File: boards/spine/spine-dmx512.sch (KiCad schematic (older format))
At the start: 27 parts, among them P2 XLR-3 Female, Q1 IRFML8244, Q2 IRFML8244, T1 10/100baseT transformer, U3 NC7WZ14, U4 NC7WZ14, U5 NC7WZ14, U6 SN75176B

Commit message: Power management and such
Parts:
- D4: value TVS 20V -> 8.5VWM; MfgId MMBZ20VALT1G -> MMBZ12VALT1G; RefPrice1k .04208 -> .04471; Vend1Id MMBZ20VALT1GOSCT-ND -> MMBZ12VALT1GOSCT-ND
- gave numbers to parts that had none: 1
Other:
- moved on the sheet: C18, C19, C20, C21, C22, C23, C24, C25, C26, C27, C28, C29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

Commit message: Clock generator, sync connectors, title blocks
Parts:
- C18, C19, C21, C22, C23, C24, C25, C26, C28: footprint 0805 -> Capacitors_SMD:C_0805
- C20, C27: footprint 1206 -> Capacitors_SMD:C_1206
- R11, R12, R13, R14: footprint (none) -> Resistors_SMD:R_0805
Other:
- note added: "A"
- note added: "Wiggle Spine board"

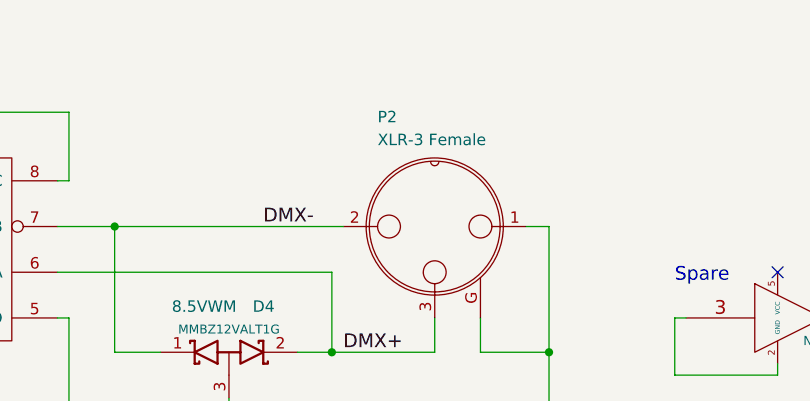
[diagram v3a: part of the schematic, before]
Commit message: Schematic footprint and refdes work
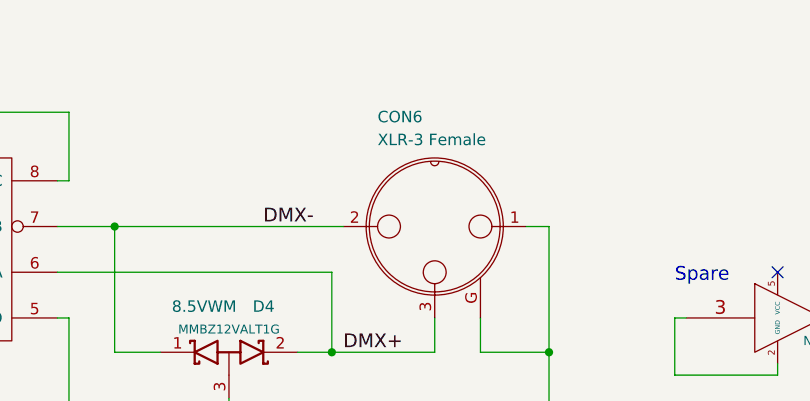
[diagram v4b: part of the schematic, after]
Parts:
- C29: footprint (none) -> Capacitors_ThroughHole:C_Rect_L13_W4_P10
- CON6: renamed from P2; footprint (none) -> Connect:XLR3MC
- D2, D3, D4, Q1, Q2: footprint (none) -> TO_SOT_Packages_SMD:SOT-23
- T1: footprint (none) -> Housings_SOIC:SOIC-16_7.5x10.3mm_Pitch1.27mm
- U3, U4, U5: footprint (none) -> TO_SOT_Packages_SMD:SC-70-6
- U6: footprint (none) -> Housings_SOIC:SOIC-8_3.9x4.9mm_Pitch1.27mm
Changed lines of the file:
@@
 F 0 "U6" H 5700 1350 60  0000 L BNN
 F 1 "SN75176B" H 5700 450 60  0000 L TNN
-F 2 "" H 6000 1300 60  0001 C CNN
+F 2 "Housings_SOIC:SOIC-8_3.9x4.9mm_Pitch1.27mm" H 6000 1300 60  0001 C CNN
 F 3 "http://www.ti.com/lit/ds/symlink/sn65176b.pdf" H 6000 1300 60  0001 C CNN
 F 4 "296-1275-1-ND" H 6000 1300 60  0001 C CNN "Vend1Id"
@@
 F 0 "T1" H 7650 4500 50  0000 L BNN
 F 1 "10/100baseT transformer" H 7650 4500 50  0001 L BNN
-F 2 "" H 8000 4450 50  0001 C CNN
+F 2 "Housings_SOIC:SOIC-16_7.5x10.3mm_Pitch1.27mm" H 8000 4450 50  0001 C CNN
 F 3 "http://www.mouser.com/ds/2/54/PT61018PEL-336005.pdf" H 8000 4300 60  0001 C CNN
 F 4 "Bourns" H 8050 4250 60  0001 C CNN "MfrId"
@@
 F 0 "U4" H 4750 2100 40  0000 C CNN
 F 1 "NC7WZ14" H 4800 1900 40  0000 C CNN
-F 2 "" H 4600 2000 60  0001 C CNN
+F 2 "TO_SOT_Packages_SMD:SC-70-6" H 4600 2000 60  0001 C CNN
 F 3 "http://www.fairchildsemi.com/datasheets/NC/NC7WZ14.pdf" H 4600 2000 60  0001 C CNN
 F 4 "0.07631" H 4600 2000 60  0001 C CNN "RefPrice1k"
@@
 F 0 "D3" V 2400 1850 50  0000 C CNN
 F 1 "BAT54 2x common cathode" H 2500 2100 50  0001 C CNN
-F 2 "" H 2500 2000 60  0001 C CNN
+F 2 "TO_SOT_Packages_SMD:SOT-23" H 2500 2000 60  0001 C CNN
 F 3 "http://www.diodes.com/_files/datasheets/ds11005.pdf" H 2500 2000 60  0001 C CNN
 F 4 "Diodes Inc" H 2500 2150 39  0001 C CNN "MfrId"
@@
 F 0 "Q1" H 5850 4500 50  0000 R CNN
 F 1 "IRFML8244" H 6150 4400 50  0001 R CNN
-F 2 "" H 5750 4550 29  0001 C CNN
+F 2 "TO_SOT_Packages_SMD:SOT-23" H 5750 4550 29  0001 C CNN
 F 3 "http://www.irf.com/product-info/datasheets/data/irfml8244pbf.pdf" H 5550 4450 60  0001 C CNN
 F 4 "Infineon" H 5550 4450 60  0001 C CNN "MfrId"
@@
 $EndComp
 $Comp
-L GND #PWR018
+L GND #PWR19
 U 1 1 563F2AEF
 P 2650 6250
-F 0 "#PWR018" H 2650 6000 50  0001 C CNN
+F 0 "#PWR19" H 2650 6000 50  0001 C CNN
 F 1 "GND" H 2650 6100 50  0000 C CNN
 F 2 "" H 2650 6250 60  0000 C CNN
@@
 $EndComp
 $Comp
-L +5V #PWR019
+L +5V #PWR18
 U 1 1 563F515D
 P 2650 3550
-F 0 "#PWR019" H 2650 3400 50  0001 C CNN
+F 0 "#PWR18" H 2650 3400 50  0001 C CNN
 F 1 "+5V" H 2650 3690 50  0000 C CNN
 F 2 "" H 2650 3550 60  0000 C CNN
@@
 F 0 "Q2" H 6250 4950 50  0000 R CNN
 F 1 "IRFML8244" H 6550 4850 50  0001 R CNN
-F 2 "" H 6150 5000 29  0001 C CNN
+F 2 "TO_SOT_Packages_SMD:SOT-23" H 6150 5000 29  0001 C CNN
 F 3 "http://www.irf.com/product-info/datasheets/data/irfml8244pbf.pdf" H 5950 4900 60  0001 C CNN
 F 4 "Infineon" H 5950 4900 60  0001 C CNN "MfrId"
@@
 $EndComp
 $Comp
-L XLR_3 P2
+L XLR_3 CON6
 U 1 1 563E82C1
 P 8050 1600
-F 0 "P2" H 7800 2050 50  0000 L BNN
+F 0 "CON6" H 7800 2050 50  0000 L BNN
 F 1 "XLR-3 Female" H 7800 1950 50  0000 L BNN
-F 2 "" H 8050 1600 60  0001 C CNN
+F 2 "Connect:XLR3MC" H 8050 1600 60  0001 C CNN
 F 3 "http://www.neutrik.us/en-us/xlr/aa-series/nc3faah2-0" H 8050 1600 60  0001 C CNN
 F 4 "568-NC3FAAH-2-O" H 8050 1600 60  0001 C CNN "Vend1Id"
@@
 F 0 "U4" H 9750 2100 40  0000 C CNN
 F 1 "NC7WZ14" H 9800 1900 40  0000 C CNN
-F 2 "" H 9600 2000 60  0001 C CNN
+F 2 "TO_SOT_Packages_SMD:SC-70-6" H 9600 2000 60  0001 C CNN
 F 3 "http://www.fairchildsemi.com/datasheets/NC/NC7WZ14.pdf" H 9600 2000 60  0001 C CNN
 F 4 "0.07631" H 9600 2000 60  0001 C CNN "RefPrice1k"
@@
 F 0 "U3" H 4100 4550 40  0000 C CNN
 F 1 "NC7WZ14" H 4150 4350 40  0000 C CNN
-F 2 "" H 3950 4450 60  0001 C CNN
+F 2 "TO_SOT_Packages_SMD:SC-70-6" H 3950 4450 60  0001 C CNN
 F 3 "http://www.fairchildsemi.com/datasheets/NC/NC7WZ14.pdf" H 3950 4450 60  0001 C CNN
 F 4 "0.07631" H 3950 4450 60  0001 C CNN "RefPrice1k"
@@
 F 0 "U3" H 4300 5000 40  0000 C CNN
 F 1 "NC7WZ14" H 4350 4800 40  0000 C CNN
-F 2 "" H 4150 4900 60  0001 C CNN
+F 2 "TO_SOT_Packages_SMD:SC-70-6" H 4150 4900 60  0001 C CNN
 F 3 "http://www.fairchildsemi.com/datasheets/NC/NC7WZ14.pdf" H 4150 4900 60  0001 C CNN
 F 4 "0.07631" H 4150 4900 60  0001 C CNN "RefPrice1k"
@@
 F 0 "U5" H 5050 5350 40  0000 C CNN
 F 1 "NC7WZ14" H 5100 5150 40  0000 C CNN
-F 2 "" H 4900 5250 60  0001 C CNN
+F 2 "TO_SOT_Packages_SMD:SC-70-6" H 4900 5250 60  0001 C CNN
 F 3 "http://www.fairchildsemi.com/datasheets/NC/NC7WZ14.pdf" H 4900 5250 60  0001 C CNN
 F 4 "0.07631" H 4900 5250 60  0001 C CNN "RefPrice1k"
@@
 F 0 "U5" H 5250 5750 40  0000 C CNN
 F 1 "NC7WZ14" H 5300 5550 40  0000 C CNN
-F 2 "" H 5100 5650 60  0001 C CNN
+F 2 "TO_SOT_Packages_SMD:SC-70-6" H 5100 5650 60  0001 C CNN
 F 3 "http://www.fairchildsemi.com/datasheets/NC/NC7WZ14.pdf" H 5100 5650 60  0001 C CNN
 F 4 "0.07631" H 5100 5650 60  0001 C CNN "RefPrice1k"
@@
 $EndComp
 $Comp
-L +5V #PWR020
+L +5V #PWR20
 U 1 1 56434028
 P 4350 6650
-F 0 "#PWR020" H 4350 6500 50  0001 C CNN
+F 0 "#PWR20" H 4350 6500 50  0001 C CNN
 F 1 "+5V" H 4350 6790 50  0000 C CNN
 F 2 "" H 4350 6650 60  0000 C CNN
@@
 	4350 6650 4350 6800
 $Comp
-L GND #PWR021
+L GND #PWR21
 U 1 1 56434123
 P 4350 7250
-F 0 "#PWR021" H 4350 7000 50  0001 C CNN
+F 0 "#PWR21" H 4350 7000 50  0001 C CNN
 F 1 "GND" H 4350 7100 50  0000 C CNN
 F 2 "" H 4350 7250 60  0000 C CNN
@@
 F 0 "D2" V 2400 950 50  0000 C CNN
 F 1 "BAT54 2x common cathode" H 2500 1200 50  0001 C CNN
-F 2 "" H 2500 1100 60  0001 C CNN
+F 2 "TO_SOT_Packages_SMD:SOT-23" H 2500 1100 60  0001 C CNN
 F 3 "http://www.diodes.com/_files/datasheets/ds11005.pdf" H 2500 1100 60  0001 C CNN
 F 4 "Diodes Inc" H 2500 1250 39  0001 C CNN "MfrId"
@@
 F 0 "C29" V 8050 6200 50  0000 L CNN
 F 1 "1nF" V 8050 5850 50  0000 L CNN
-F 2 "" H 8138 5950 30  0001 C CNN
+F 2 "Capacitors_ThroughHole:C_Rect_L13_W4_P10" H 8138 5950 30  0001 C CNN
 F 3 "http://en.tdk.eu/inf/20/20/db/fc_2009/Y2_B32021_026.pdf" H 8100 6100 60  0001 C CNN
 F 4 "Digikey" H 8100 6100 60  0001 C CNN "Vend1"
@@
 F 0 "D4" H 7350 2350 50  0000 R CNN
 F 1 "8.5VWM" H 6900 2350 50  0000 L CNN
-F 2 "" H 7150 2150 60  0001 C CNN
+F 2 "TO_SOT_Packages_SMD:SOT-23" H 7150 2150 60  0001 C CNN
 F 3 "http://www.onsemi.com/pub_link/Collateral/MMBZ5V6ALT1-D.PDF" H 7150 2150 60  0001 C CNN
 F 4 "ON Semi" H 6800 2300 39  0001 L BNN "MfrId"
@@
 FB 59 00 E6 A5 69 3A 37 9E CF 73 BC F7 37 E3 33 5D 9E A8 3E 7F 80 FA F7 F6 BB 44 F4 6E D4 E7 77
 A2 1E 1F 27 A2 E3 16 70 32 E9 54 FE 3F E7 AF 00 CA 1C A3 36 0A 00 00 00 00 49 45 4E 44 AE 42 60
-82 70
+82 FF
 EndData
 $EndBitmap

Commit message: Simpler indicator LED strategy
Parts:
- U3, U4, U5: footprint TO_SOT_Packages_SMD:SC-70-6 -> TO_SOT_Packages_SMD:SOT-23-6
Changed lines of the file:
@@
 F 0 "U4" H 4750 2100 40  0000 C CNN
 F 1 "NC7WZ14" H 4800 1900 40  0000 C CNN
-F 2 "TO_SOT_Packages_SMD:SC-70-6" H 4600 2000 60  0001 C CNN
+F 2 "TO_SOT_Packages_SMD:SOT-23-6" H 4600 2000 60  0001 C CNN
 F 3 "http://www.fairchildsemi.com/datasheets/NC/NC7WZ14.pdf" H 4600 2000 60  0001 C CNN
 F 4 "0.07631" H 4600 2000 60  0001 C CNN "RefPrice1k"
@@
 F 0 "U3" H 4100 4550 40  0000 C CNN
 F 1 "NC7WZ14" H 4150 4350 40  0000 C CNN
-F 2 "TO_SOT_Packages_SMD:SC-70-6" H 3950 4450 60  0001 C CNN
+F 2 "TO_SOT_Packages_SMD:SOT-23-6" H 3950 4450 60  0001 C CNN
 F 3 "http://www.fairchildsemi.com/datasheets/NC/NC7WZ14.pdf" H 3950 4450 60  0001 C CNN
 F 4 "0.07631" H 3950 4450 60  0001 C CNN "RefPrice1k"
@@
 F 0 "U3" H 4300 5000 40  0000 C CNN
 F 1 "NC7WZ14" H 4350 4800 40  0000 C CNN
-F 2 "TO_SOT_Packages_SMD:SC-70-6" H 4150 4900 60  0001 C CNN
+F 2 "TO_SOT_Packages_SMD:SOT-23-6" H 4150 4900 60  0001 C CNN
 F 3 "http://www.fairchildsemi.com/datasheets/NC/NC7WZ14.pdf" H 4150 4900 60  0001 C CNN
 F 4 "0.07631" H 4150 4900 60  0001 C CNN "RefPrice1k"
@@
 F 0 "U5" H 5050 5350 40  0000 C CNN
 F 1 "NC7WZ14" H 5100 5150 40  0000 C CNN
-F 2 "TO_SOT_Packages_SMD:SC-70-6" H 4900 5250 60  0001 C CNN
+F 2 "TO_SOT_Packages_SMD:SOT-23-6" H 4900 5250 60  0001 C CNN
 F 3 "http://www.fairchildsemi.com/datasheets/NC/NC7WZ14.pdf" H 4900 5250 60  0001 C CNN
 F 4 "0.07631" H 4900 5250 60  0001 C CNN "RefPrice1k"
@@
 FB 59 00 E6 A5 69 3A 37 9E CF 73 BC F7 37 E3 33 5D 9E A8 3E 7F 80 FA F7 F6 BB 44 F4 6E D4 E7 77
 A2 1E 1F 27 A2 E3 16 70 32 E9 54 FE 3F E7 AF 00 CA 1C A3 36 0A 00 00 00 00 49 45 4E 44 AE 42 60
-82 FF
+82 00
 EndData
 $EndBitmap
@@
 72 0F 1C A9 DC 70 49 CB 79 33 88 85 99 AD 01 6C 4B 10 FC 3B 13 DE 3B 37 68 79 AD 07 BC 00 3C 0E
 3C 31 EE E3 D8 E7 0F 03 D7 7B 9F FB C1 E1 FF 01 18 C4 96 1D B8 0E 40 07 00 00 00 00 49 45 4E 44
-AE 42 60 82 00
+AE 42 60 82 84
 EndData
 $EndBitmap

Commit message: Fix some 6-pin packages
I had several of these mislabeled as SOT23-6, but there are no SOT23-6 parts here. The LDOs are SOT23-5, and the others (TVS diode array and inverters) are in the smaller SC-88 package.
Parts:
- U3, U4, U5: footprint TO_SOT_Packages_SMD:SOT-23-6 -> TO_SOT_Packages_SMD:SC-70-6
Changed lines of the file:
@@
 F 0 "U4" H 4750 2100 40  0000 C CNN
 F 1 "NC7WZ14" H 4800 1900 40  0000 C CNN
-F 2 "TO_SOT_Packages_SMD:SOT-23-6" H 4600 2000 60  0001 C CNN
+F 2 "TO_SOT_Packages_SMD:SC-70-6" H 4600 2000 60  0001 C CNN
 F 3 "http://www.fairchildsemi.com/datasheets/NC/NC7WZ14.pdf" H 4600 2000 60  0001 C CNN
 F 4 "0.07631" H 4600 2000 60  0001 C CNN "RefPrice1k"
@@
 $EndComp
 $Comp
-L GND #PWR19
+L GND #PWR018
 U 1 1 563F2AEF
 P 2650 6250
-F 0 "#PWR19" H 2650 6000 50  0001 C CNN
+F 0 "#PWR018" H 2650 6000 50  0001 C CNN
 F 1 "GND" H 2650 6100 50  0000 C CNN
 F 2 "" H 2650 6250 60  0000 C CNN
@@
 $EndComp
 $Comp
-L +5V #PWR18
+L +5V #PWR019
 U 1 1 563F515D
 P 2650 3550
-F 0 "#PWR18" H 2650 3400 50  0001 C CNN
+F 0 "#PWR019" H 2650 3400 50  0001 C CNN
 F 1 "+5V" H 2650 3690 50  0000 C CNN
 F 2 "" H 2650 3550 60  0000 C CNN
@@
 F 0 "U3" H 4100 4550 40  0000 C CNN
 F 1 "NC7WZ14" H 4150 4350 40  0000 C CNN
-F 2 "TO_SOT_Packages_SMD:SOT-23-6" H 3950 4450 60  0001 C CNN
+F 2 "TO_SOT_Packages_SMD:SC-70-6" H 3950 4450 60  0001 C CNN
 F 3 "http://www.fairchildsemi.com/datasheets/NC/NC7WZ14.pdf" H 3950 4450 60  0001 C CNN
 F 4 "0.07631" H 3950 4450 60  0001 C CNN "RefPrice1k"
@@
 F 0 "U3" H 4300 5000 40  0000 C CNN
 F 1 "NC7WZ14" H 4350 4800 40  0000 C CNN
-F 2 "TO_SOT_Packages_SMD:SOT-23-6" H 4150 4900 60  0001 C CNN
+F 2 "TO_SOT_Packages_SMD:SC-70-6" H 4150 4900 60  0001 C CNN
 F 3 "http://www.fairchildsemi.com/datasheets/NC/NC7WZ14.pdf" H 4150 4900 60  0001 C CNN
 F 4 "0.07631" H 4150 4900 60  0001 C CNN "RefPrice1k"
@@
 F 0 "U5" H 5050 5350 40  0000 C CNN
 F 1 "NC7WZ14" H 5100 5150 40  0000 C CNN
-F 2 "TO_SOT_Packages_SMD:SOT-23-6" H 4900 5250 60  0001 C CNN
+F 2 "TO_SOT_Packages_SMD:SC-70-6" H 4900 5250 60  0001 C CNN
 F 3 "http://www.fairchildsemi.com/datasheets/NC/NC7WZ14.pdf" H 4900 5250 60  0001 C CNN
 F 4 "0.07631" H 4900 5250 60  0001 C CNN "RefPrice1k"
@@
 $EndComp
 $Comp
-L +5V #PWR20
+L +5V #PWR020
 U 1 1 56434028
 P 4350 6650
-F 0 "#PWR20" H 4350 6500 50  0001 C CNN
+F 0 "#PWR020" H 4350 6500 50  0001 C CNN
 F 1 "+5V" H 4350 6790 50  0000 C CNN
 F 2 "" H 4350 6650 60  0000 C CNN
@@
 	4350 6650 4350 6800
 $Comp
-L GND #PWR21
+L GND #PWR021
 U 1 1 56434123
 P 4350 7250
-F 0 "#PWR21" H 4350 7000 50  0001 C CNN
+F 0 "#PWR021" H 4350 7000 50  0001 C CNN
 F 1 "GND" H 4350 7100 50  0000 C CNN
 F 2 "" H 4350 7250 60  0000 C CNN
@@
 FB 59 00 E6 A5 69 3A 37 9E CF 73 BC F7 37 E3 33 5D 9E A8 3E 7F 80 FA F7 F6 BB 44 F4 6E D4 E7 77
 A2 1E 1F 27 A2 E3 16 70 32 E9 54 FE 3F E7 AF 00 CA 1C A3 36 0A 00 00 00 00 49 45 4E 44 AE 42 60
-82 00
+82 4F
 EndData
 $EndBitmap
@@
 72 0F 1C A9 DC 70 49 CB 79 33 88 85 99 AD 01 6C 4B 10 FC 3B 13 DE 3B 37 68 79 AD 07 BC 00 3C 0E
 3C 31 EE E3 D8 E7 0F 03 D7 7B 9F FB C1 E1 FF 01 18 C4 96 1D B8 0E 40 07 00 00 00 00 49 45 4E 44
-AE 42 60 82 84
+AE 42 60 82 00
 EndData
 $EndBitmap

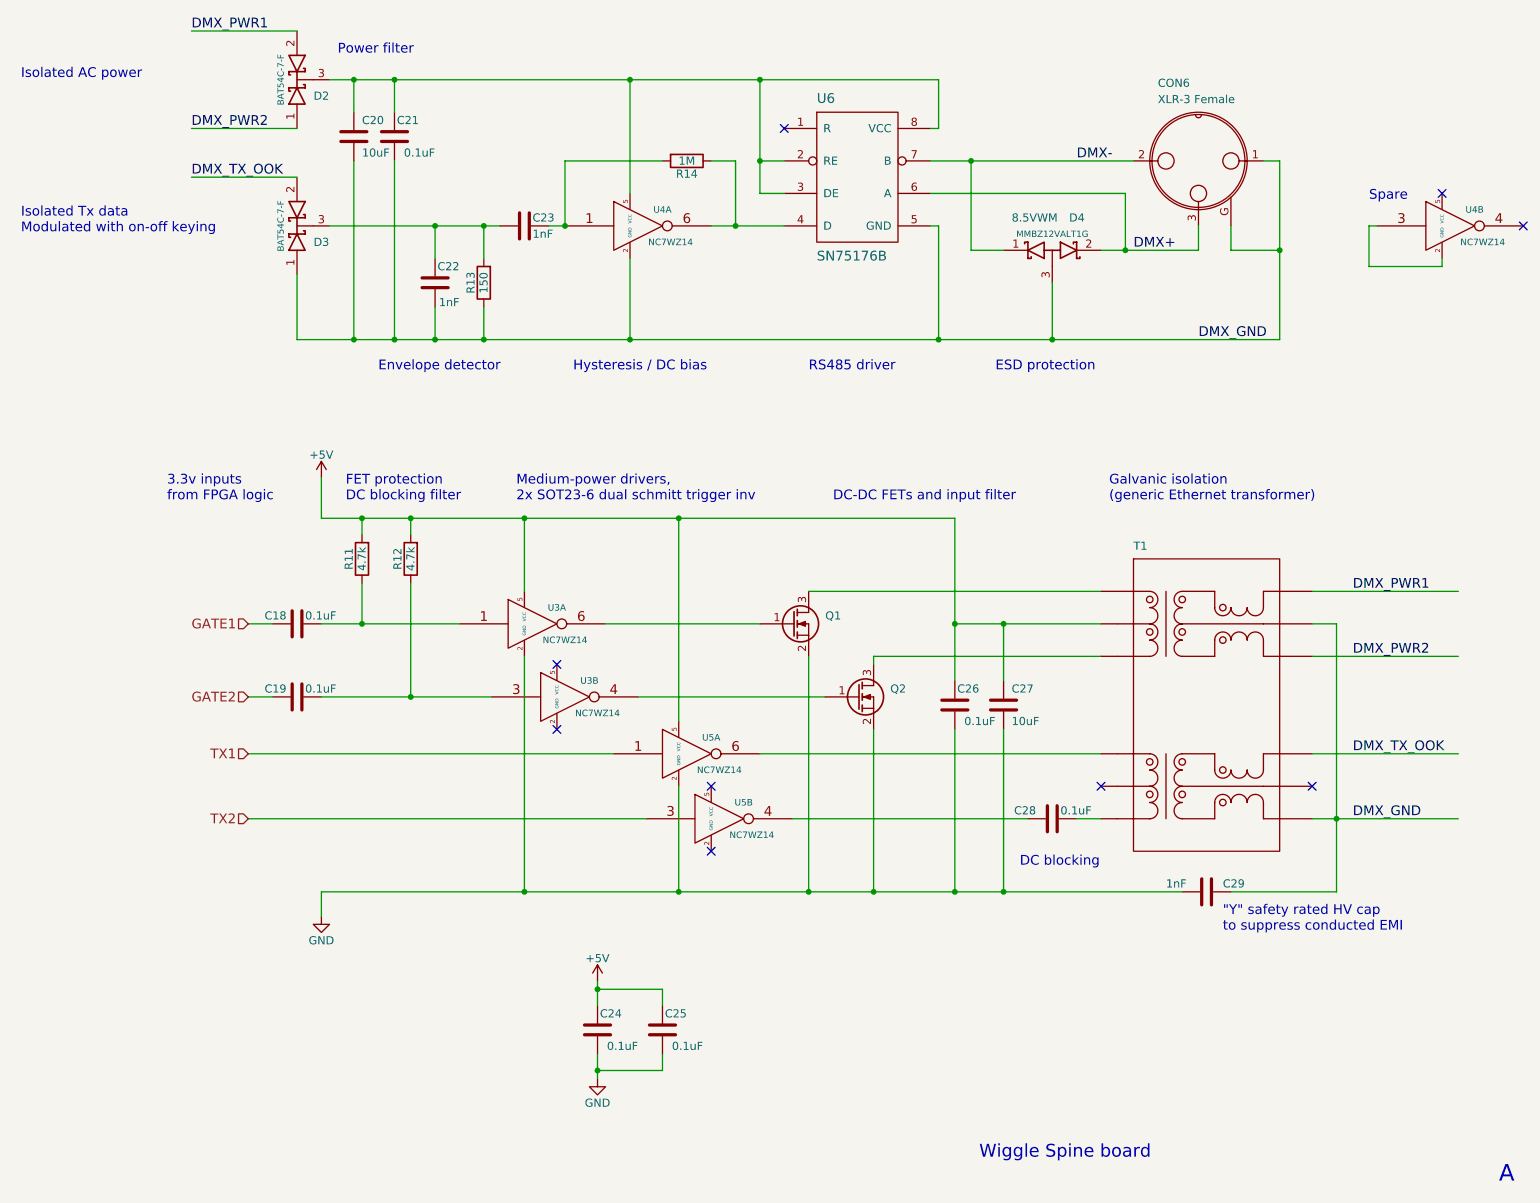
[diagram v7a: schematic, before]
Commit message: First round of DMX isolator simplifications
- Removed RC filters on gate drive; they aren't accurate enough to prevent the FPGA from destroying the FETs with bad drive frequencies or duty cycles. I'm planning on spec'ing a polyfuse to protect this circuit instead. Leaving in the DC blocking cap on the signal side, since the inverter output impedance is high enough it probably wouldn't reliably trigger a polyfuse before breaking.

- Removed fancypants schmitt trigger nonsense in the demodulator. This was just oscillating and wasn't working like it did in simulation at all, but it turns out we can just use the '485 driver input directly. The peak detector output is plenty strong with a 6 MHz carrier.

- Other changes still todo... output voltage is about 0.75V lower than spec. It still works, but I don't like it. There's plenty of extra energy coming through the transformer, going to try a full wave rectifier instead.
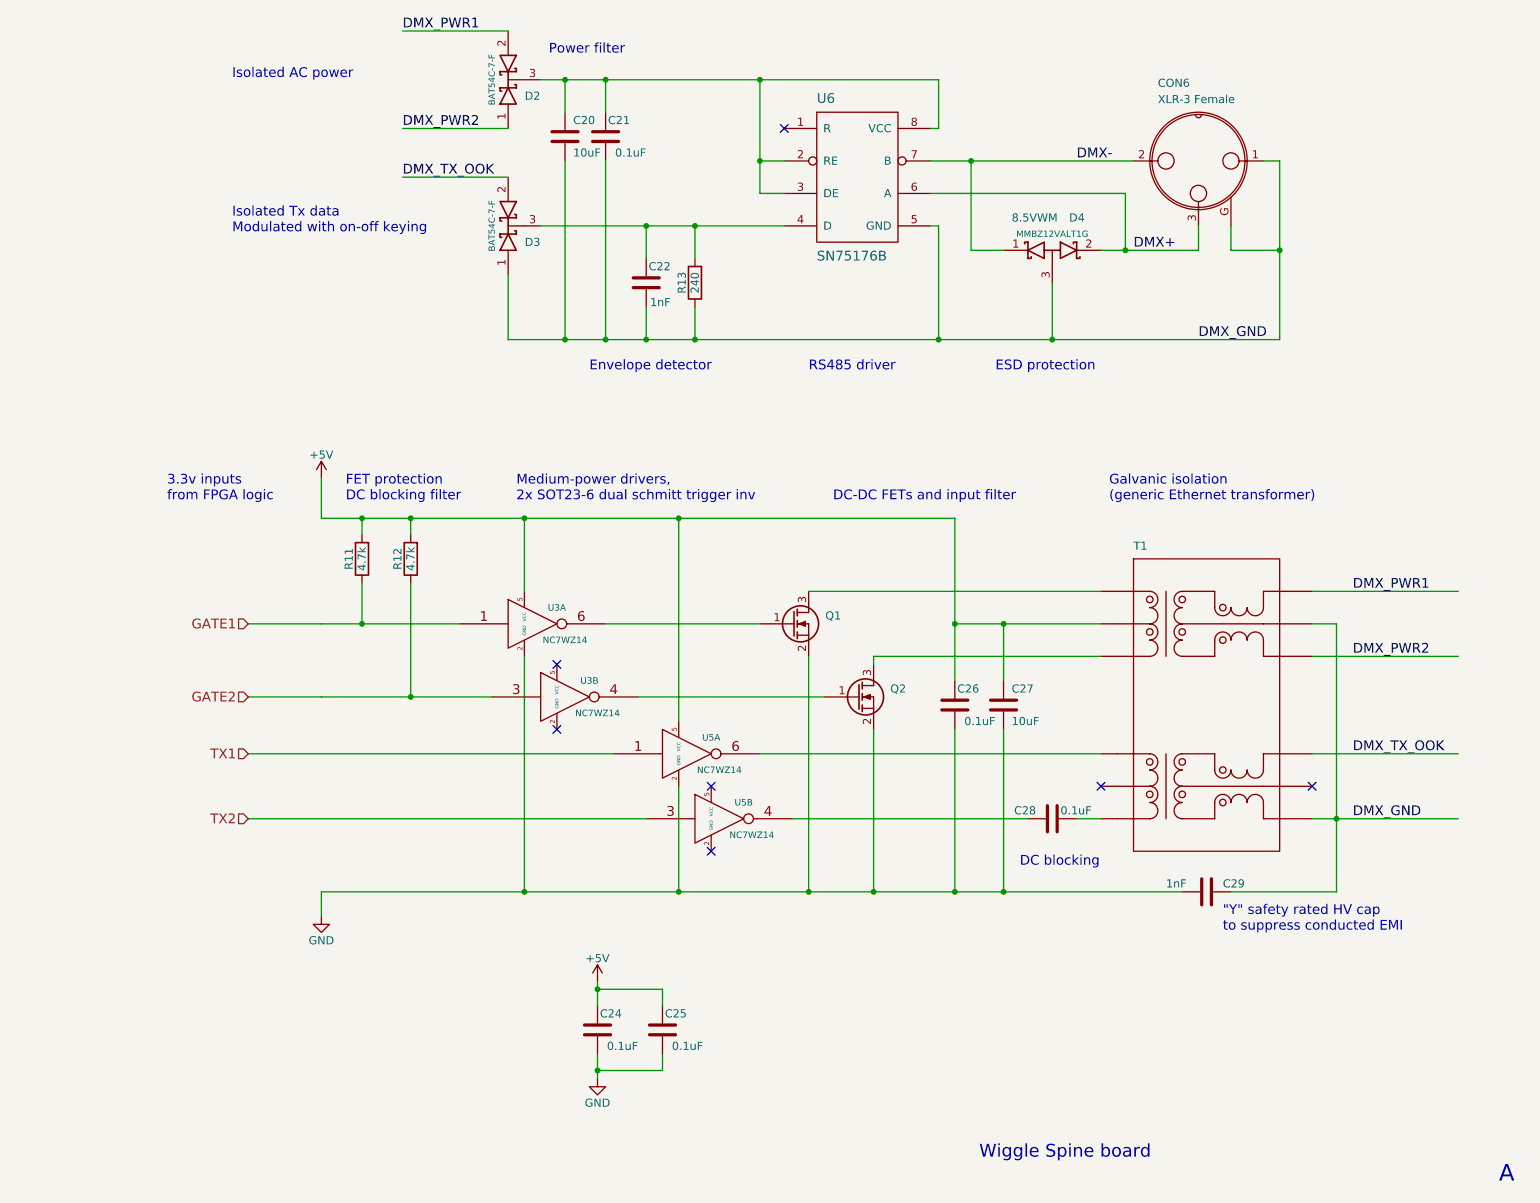
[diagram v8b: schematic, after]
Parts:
- removed C18, C19: 0.1uF, Capacitors_SMD:C_0805, symbol C
- removed C23: 1nF, Capacitors_SMD:C_0805, symbol C
- removed R14: 1M, Resistors_SMD:R_0805, symbol R
- removed U4: NC7WZ14, TO_SOT_Packages_SMD:SC-70-6, symbol NC7WZ14
- R13: value 150 -> 240; MfgId RMCF0805JT150R -> RMCF0805JT240R; Vend1Id RMCF0805JT150RCT-ND -> RMCF0805JT240RCT-ND
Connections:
- wire segments 92 -> 113
- no-connect marks 9 -> 7
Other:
- note removed: "Hysteresis / DC bias"
- note removed: "Spare"
- moved on the sheet: C20, C21, C22, D2, D3, R13
